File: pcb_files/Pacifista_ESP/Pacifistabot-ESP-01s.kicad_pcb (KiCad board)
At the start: 2 copper layers, 42 x 48.1 mm, 32 parts, among them J1 Conn_01x01, J10 Conn_01x03, J11 Conn_01x03, J2 Conn_01x01, J3 Conn_01x09, J4 Conn_01x06, J5 Conn_01x06, J6 Conn_01x06, J7 Conn_01x06, J8 Conn_01x06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

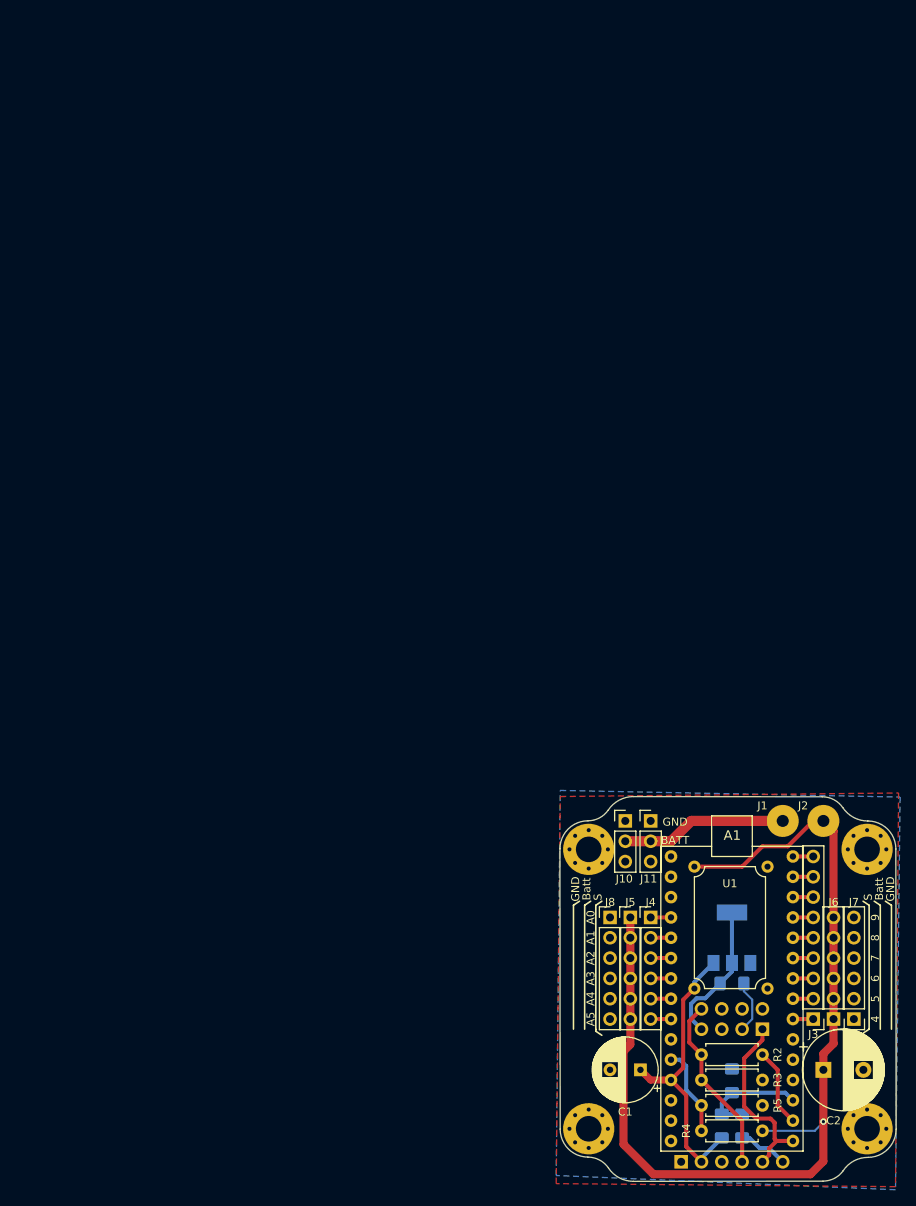
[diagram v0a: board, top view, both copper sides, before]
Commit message: Corrección de los pines de la PCB y el logo de DB
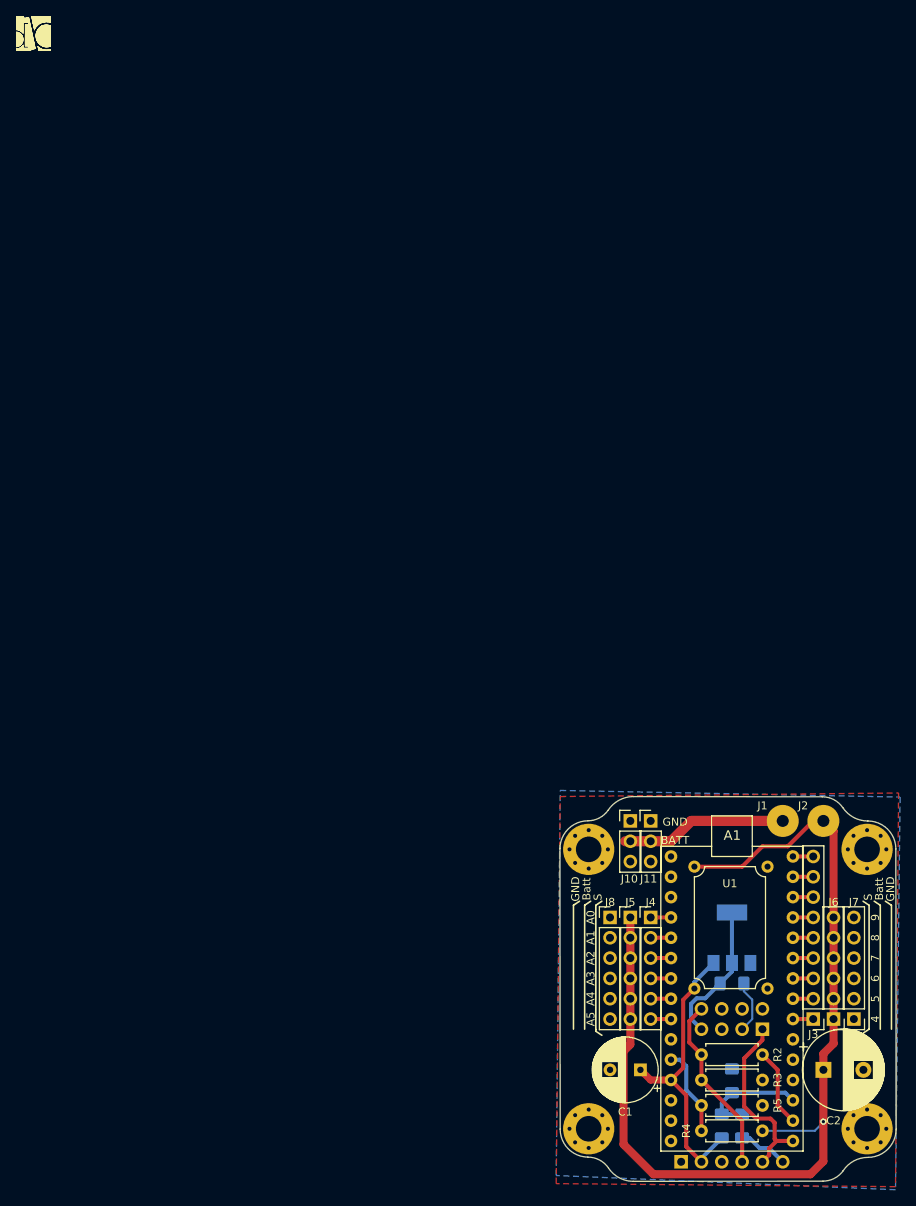
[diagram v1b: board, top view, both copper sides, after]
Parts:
- added G*** (x3): LOGO, Pacifista_ESP:LogoDB, F.Cu at (0.00, 0.00)
- moved J10 0.63 mm to (73.7, 98.4)

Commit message: Creación de alhambra
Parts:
- removed the G*** at (0.00, 0.00) (x3)
